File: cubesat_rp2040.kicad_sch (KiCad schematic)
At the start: 0 parts

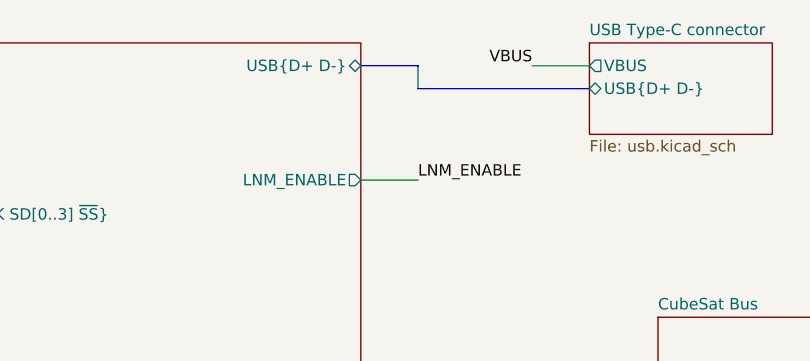
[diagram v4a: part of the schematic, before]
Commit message: Update footprints, route more circuit blocks
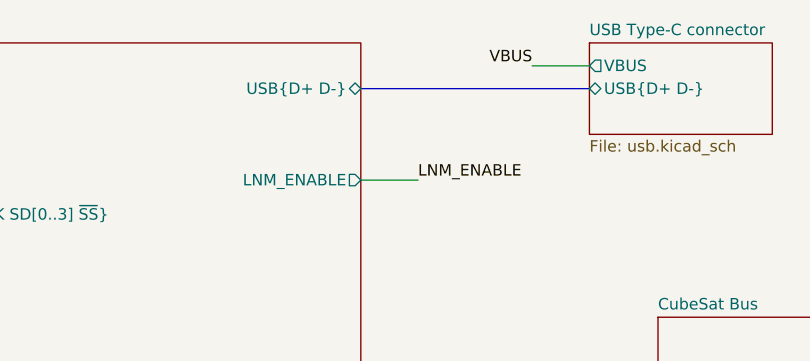
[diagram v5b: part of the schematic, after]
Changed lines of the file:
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@@
 	(bus
 		(pts
-			(xy 177.8 57.15) (xy 171.45 57.15)
+			(xy 171.45 59.69) (xy 196.85 59.69)
+		)
+		(stroke
+			(width 0)
+			(type default)
+		)
+	)
+	(wire
+		(pts
+			(xy 63.5 93.98) (xy 69.85 93.98)
+		)
+		(stroke
+			(width 0)
+			(type default)
+		)
+	)
+	(wire
+		(pts
+			(xy 95.25 93.98) (xy 107.95 93.98)
 		)
 		(stroke
@@
 	(bus
 		(pts
-			(xy 177.8 59.69) (xy 177.8 57.15)
-		)
-		(stroke
-			(width 0)
-			(type default)
-		)
-	)
-	(wire
-		(pts
-			(xy 63.5 93.98) (xy 69.85 93.98)
-		)
-		(stroke
-			(width 0)
-			(type default)
-		)
-	)
-	(wire
-		(pts
-			(xy 95.25 93.98) (xy 107.95 93.98)
+			(xy 95.25 73.66) (xy 120.65 73.66)
+		)
+		(stroke
+			(width 0)
+			(type default)
+		)
+	)
+	(wire
+		(pts
+			(xy 107.95 93.98) (xy 120.65 93.98)
 		)
 		(stroke
@@
 	(bus
 		(pts
-			(xy 95.25 73.66) (xy 120.65 73.66)
-		)
-		(stroke
-			(width 0)
-			(type default)
-		)
-	)
-	(wire
-		(pts
-			(xy 107.95 93.98) (xy 120.65 93.98)
-		)
-		(stroke
-			(width 0)
-			(type default)
-		)
-	)
-	(bus
-		(pts
 			(xy 95.25 124.46) (xy 114.3 124.46)
 		)
@@
 		(pts
 			(xy 95.25 109.22) (xy 107.95 109.22)
-		)
-		(stroke
-			(width 0)
-			(type default)
-		)
-	)
-	(bus
-		(pts
-			(xy 196.85 59.69) (xy 177.8 59.69)
 		)
 		(stroke
@@
 		)
 		(pin "USB{D+ D-}" bidirectional
-			(at 171.45 57.15 0)
-			(effects
-				(font
+			(at 171.45 59.69 0)
+			(effects
+				(font

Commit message: Big update, bad commit messsage :)
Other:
- sheet Crystal oscillator renamed Oscillator
- sheet Power renamed VBUS to 3V3
- sheet USB Type-C connector renamed USB Type C connector
- added sheet USB 2.0 Hub (TUSB4041I_4-port_USB20_hub.kicad_sch)
- sheet Debug ports: added {SWCLK SWDIO}, ~{RESET}; removed RUN, {SWDCLK SWDIO}
- sheet Oscillator: file xo.kicad_sch -> RST3225N_TCXO_32M0.kicad_sch
- sheet Oscillator ports: added F_{out}; removed XIN, XOUT
- sheet RP2040 ports: added {SWCLK SWDIO}; removed XOUT, {SWDCLK SWDIO}
- sheet Reset button ports: added ~{RESET}; removed RUN
- sheet USB Type C connector ports: added USB_UP{D+ D-}; removed USB{D+ D-}
- sheet VBUS to 3V3: file power.kicad_sch -> L7983_5V_stepdown_3V3.kicad_sch
- sheet VBUS to 3V3 ports: added ~{RESET}; removed ~{RST}
- company: (none) -> Magnus Oksbøl Therkelsen

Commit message: Major update, everything has been touched
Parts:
- added C101: 100n, cubesat_rp2040:C_0402_1005Metric, symbol Device:C
- added H101, H102, H103, H104: MountingHole_Pad, MountingHole:MountingHole_3.2mm_M3_Pad_Via, symbol Mechanical:MountingHole_Pad
- added J101: Conn_01x02, Connector_PinHeader_2.54mm:PinHeader_1x02_P2.54mm_Horizontal, symbol Connector_Generic:Conn_01x02
- added J102, J103: ESQ-126-39-G-D, cubesat_rp2040:SAMTEC_ESQ-126-39-G-D, symbol cubesat_rp2040:ESQ-126-39-G-D
- added R101: 100k, cubesat_rp2040:R_0402_1005Metric, symbol Device:R
- added R102: 10k, cubesat_rp2040:R_0402_1005Metric, symbol Device:R
- added SW101: SW_Push, Button_Switch_SMD:SW_SPST_B3U-1000P, symbol Switch:SW_Push
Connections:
- net +3V3: now also R101.1
- new net: R101.2, R102.2, SW101.2
- new net +5V: J102.25, J102.26, J103.25, J103.26
- new net CAN_A.N: J103.01
- new net CAN_A.P: J103.03
- new net CAN_B.N: J103.02
- new net CAN_B.P: J103.04
- new net CHARGE: J103.31, J103.32
- new net GND: C101.2, H101.1, H102.1, H103.1, H104.1, J101.2 (Pin_2), J102.29, J102.30, J102.31, J102.32, J103.33, J103.34, SW101.1
- new net UART_A.RX: J103.07
- new net UART_A.TX: J103.05
- new net UART_B.RX: J103.08
- new net UART_B.TX: J103.06
- new net UART_C.RX: J103.15
- new net UART_C.TX: J103.13
- new net UART_D.RX: J103.24
- new net UART_D.TX: J103.22
- new net VBAT: J102.45, J102.46
- new net ~{RESET}: C101.1, R102.1
- new net ~{USB_BOOT}: J101.1 (Pin_1)
- no-connect marks 0 -> 85
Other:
- sheet RP2040 renamed RP2040 - Unit 1
- sheet USB Type C connector renamed USB
- sheet VBUS to 3V3 renamed Power
- removed sheet CubeSat Bus
- removed sheet Debug
- removed sheet Flash
- removed sheet Reset button
- removed sheet USB 2.0 Hub
- added sheet RP2040 - Unit 2 (rp2040.kicad_sch)
- added sheet RP2040 - Unit 3 (rp2040.kicad_sch)
- sheet RP2040 - Unit 1 ports: added 48M0_CLK, ADC0, ADC1, ADC2, ADC3, CAN_A{N P}, CAN_B{N P}, USB_VBUS_DET, ~{USB_BOOT}; removed QSPI{SCLK SD[0..3] ~{SS}}, XIN, {SWCLK SWDIO}
- sheet USB ports: added PWRCTL0/BATEN0, PWRCTL1/BATEN1, PWRCTL2/BATEN2, PWRCTL3/BATEN3, USB_DN0{D+ D-}, USB_DN1{D+ D-}, USB_DN2{D+ D-}, USB_DN3{D+ D-}, XIN, ~{RESET}; removed USB_UP{D+ D-}, VBUS
- note added: "Not sure if mounting holes should be connected to ground. Is there potential for ground loops?"

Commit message: Another large revision, but we are getting closer
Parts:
- added D1, D10, D11, D12, D2, D3, D4, D5, D6, D7, D8, D9: D_TVS, Diode_SMD:D_0402_1005Metric, symbol Device:D_TVS
- C1: renamed from C101; value 100n -> 100nF; LCSC_Part_Number (none) -> C960916; MANUFACTURER (none) -> Samsung Electro-Mechanics; Manufacturer_Part_Number CL31B104KBCNNNC -> CL05B104KB5NNNC
- J1: renamed from J101; LCSC_Part_Number (none) -> C7501290; Manufacturer_Name (none) -> Megastar; Manufacturer_Part_Number (none) -> ZX-PZ2.54-1-2PWZ
- J2: renamed from J103; footprint cubesat_rp2040:SAMTEC_ESQ-126-39-G-D -> cubesat_rp2040:SAMTEC_ESQ-126-39-G-D_CUBESAT; LCSC_Part_Number (none) -> C7466599
- J3: renamed from J102; footprint cubesat_rp2040:SAMTEC_ESQ-126-39-G-D -> cubesat_rp2040:SAMTEC_ESQ-126-39-G-D_CUBESAT; LCSC_Part_Number (none) -> C7466599
- R1: renamed from R101; value 100k -> 100kR; LCSC_Part_Number (none) -> C191569; Manufacturer_Name Vishay -> PANASONIC; Manufacturer_Part_Number P-0402E1003FGxx -> ERA2AED104X
- R2: renamed from R102; value 10k -> 10kR; LCSC_Part_Number (none) -> C191568; Manufacturer_Name Vishay -> PANASONIC; Manufacturer_Part_Number P-0402E1002FGxx -> ERA2AED103X
- SW1: renamed from SW101; footprint Button_Switch_SMD:SW_SPST_B3U-1000P -> cubesat_rp2040:SW_Push_SPST_XKB_TS-1101-X-X; LCSC_Part_Number (none) -> C318938; Manufacturer_Name (none) -> XKB Connection; Manufacturer_Part_Number (none) -> TS-1101-C-W
- renumbered H101 to H1, H102 to H2, H103 to H3, H104 to H4
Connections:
- net +3V3: now also J2.27, J2.28
- net CAN_A.N: now also D6.2 (A2)
- net CAN_A.P: now also D5.2 (A2)
- net CAN_B.N: now also D7.2 (A2)
- net CAN_B.P: now also D8.2 (A2)
- net GND: now also D1.1 (A1), D10.1 (A1), D11.1 (A1), D12.1 (A1), D2.1 (A1), D3.1 (A1), D4.1 (A1), D5.1 (A1), D6.1 (A1), D7.1 (A1), D8.1 (A1), D9.1 (A1)
- net UART_A.RX renamed UART_A.D-
- net UART_A.D-: now also D3.2 (A2)
- net UART_A.TX renamed UART_A.D+
- net UART_A.D+: now also D4.2 (A2)
- net UART_B.RX renamed UART_B.D-
- net UART_B.D-: now also D10.2 (A2)
- net UART_B.TX renamed UART_B.D+
- net UART_B.D+: now also D9.2 (A2)
- net UART_C.RX renamed UART_C.D-
- net UART_C.D-: now also D1.2 (A2)
- net UART_C.TX renamed UART_C.D+
- net UART_C.D+: now also D2.2 (A2)
- net UART_D.RX renamed UART_D.D-
- net UART_D.D-: now also D12.2 (A2)
- net UART_D.TX renamed UART_D.D+
- net UART_D.D+: now also D11.2 (A2)
- net ~{RESET} renamed ~{USR_RESET}
- no-connect marks 85 -> 84
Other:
- sheet RP2040 - Unit 1 renamed RP2040 - Unit A
- sheet RP2040 - Unit 2 renamed RP2040 - Unit B
- sheet RP2040 - Unit 3 renamed RP2040 - Unit C
- removed sheet Power
- added sheet LVDS (lvds.kicad_sch)
- added sheet TMR voting (tmr_voting.kicad_sch)
- sheet Oscillator ports: added 24M0_CLK; removed F_{out}
- sheet RP2040 - Unit A ports: added 24M0_CLK, CAN_A{P N}, CAN_B{P N}, VOTE_1, VOTE_2; removed 48M0_CLK, ADC0, ADC1, ADC2, ADC3, CAN_A{N P}, CAN_B{N P}, LNM_ENABLE, RUN
- sheet RP2040 - Unit B ports: added 24M0_CLK, CAN_A{P N}, CAN_B{P N}, VOTE_1, VOTE_2; removed 48M0_CLK, ADC0, ADC1, ADC2, ADC3, CAN_A{N P}, CAN_B{N P}, LNM_ENABLE, RUN
- sheet RP2040 - Unit C ports: added 24M0_CLK, CAN_A{P N}, CAN_B{P N}, VOTE_1, VOTE_2; removed 48M0_CLK, ADC0, ADC1, ADC2, ADC3, CAN_A{N P}, CAN_B{N P}, LNM_ENABLE, RUN
- sheet USB ports: added CLK_24MHz, PWRCTL4/BATEN4, USB_DN4{D+ D-}; removed PWRCTL0/BATEN0, USB_DN0{D+ D-}, XIN
- moved on the sheet: C1, H1, H2, H3, H4, J1, J2, J3, R1, R2, SW1
